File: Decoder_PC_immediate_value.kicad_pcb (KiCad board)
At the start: 4 copper layers, 81.4 x 51.2 mm, 27 parts, among them Q1 BC818

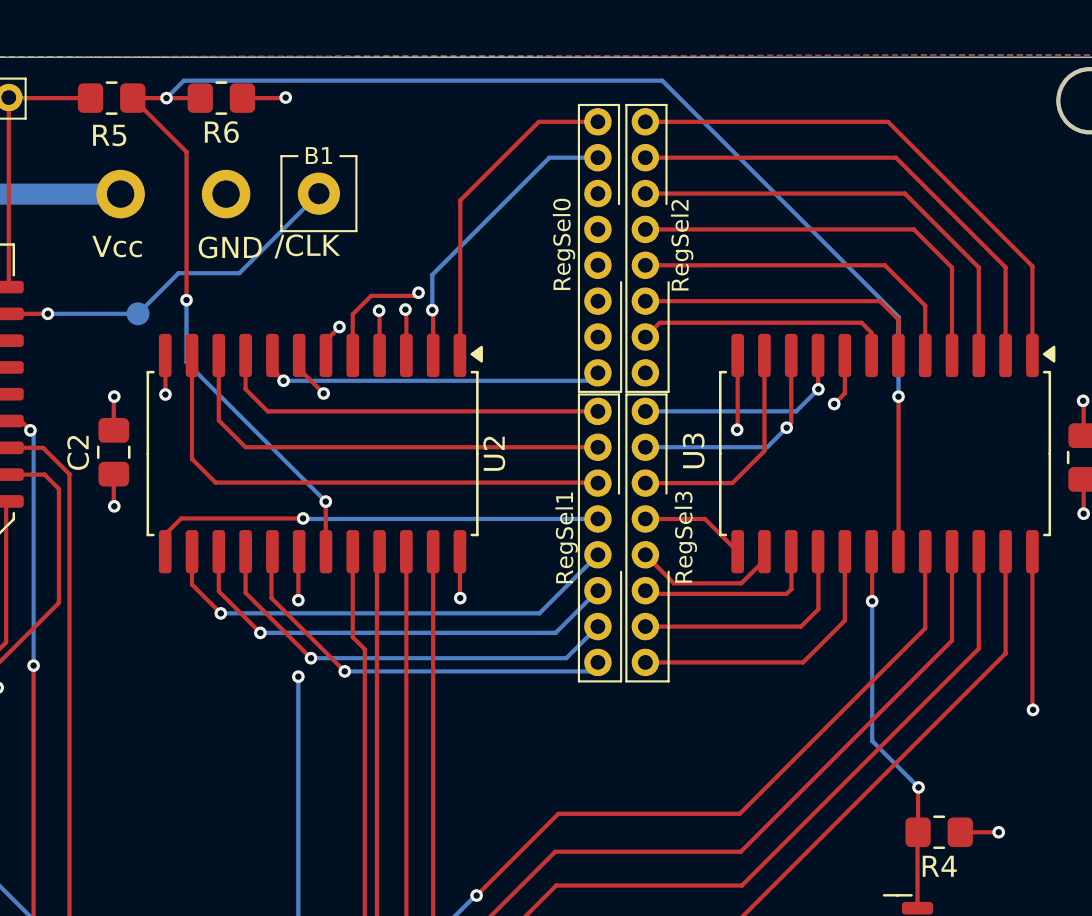
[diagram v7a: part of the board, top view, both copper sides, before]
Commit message: Added Test Points
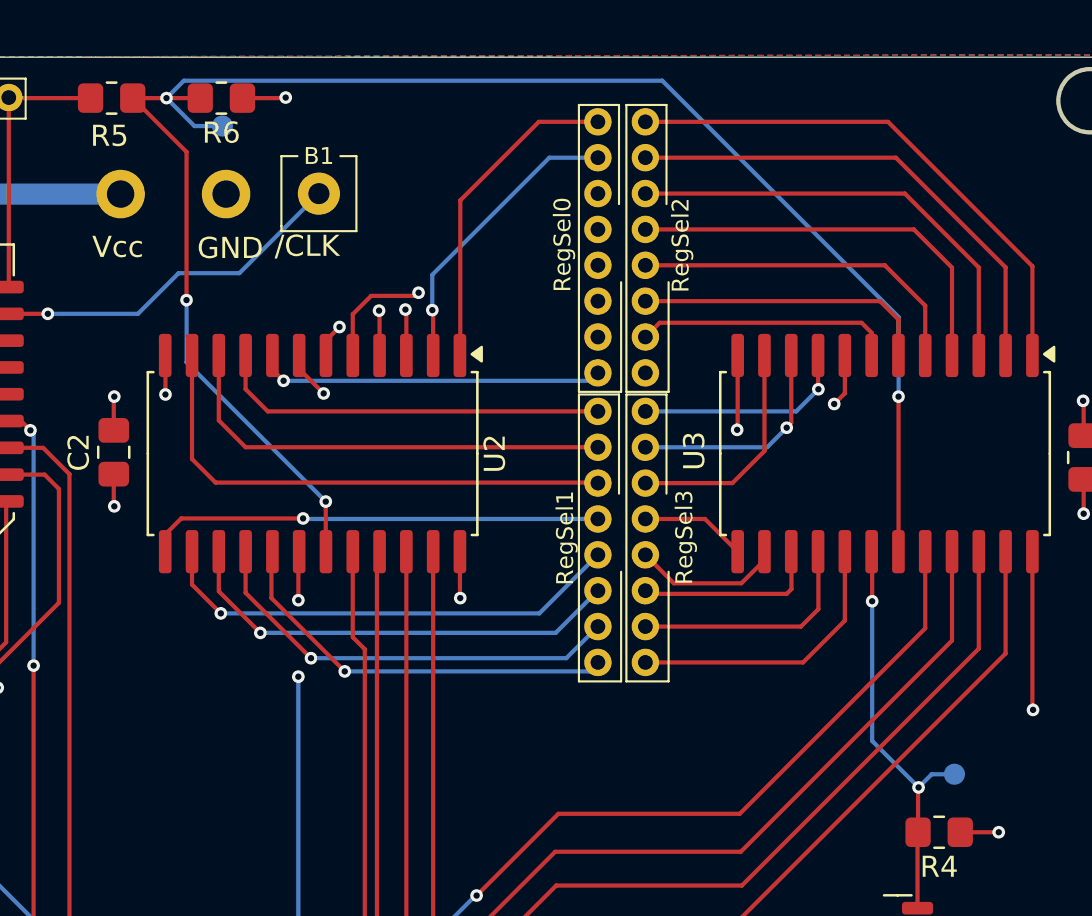
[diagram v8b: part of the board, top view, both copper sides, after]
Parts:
- added TP4: /REG_ACT, TestPoint:TestPoint_Pad_D1.0mm, B.Cu at (110.4, 62.5)
- added TP5: /REG4, TestPoint:TestPoint_Pad_D1.0mm, B.Cu at (145.1, 93.2)
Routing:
- net /REG_ACT: track 79.3 -> 82.5 mm
- net /REG4: track 17.8 -> 19.8 mm
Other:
- board text added: "/REG[4]"
- board text added: "/REG_ACT"
